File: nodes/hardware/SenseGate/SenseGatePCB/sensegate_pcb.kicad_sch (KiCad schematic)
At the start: 6 parts, among them J1 Conn_01x04_Socket, J2 Conn_01x04_Socket, J3 Conn_01x04_Socket, SW1 SW_Reed, SW2 SW_Reed, SW3 SW_Reed

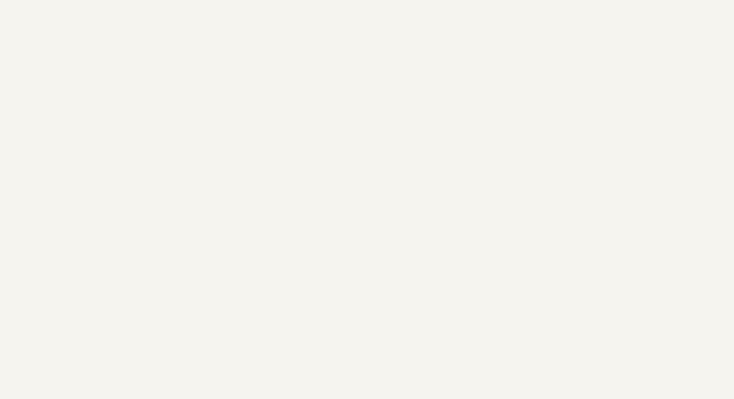
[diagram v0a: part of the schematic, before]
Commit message: added symbol for solar dcdc converter
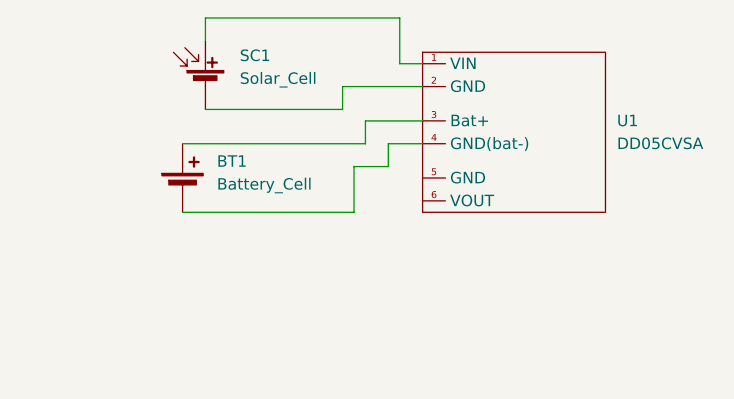
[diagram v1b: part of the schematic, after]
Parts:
- added BT1: Battery_Cell, symbol Device:Battery_Cell
- added SC1: Solar_Cell, symbol Device:Solar_Cell
- added U1: DD05CVSA, symbol custom_symbols:dd05cvsa_DCDC_Converter
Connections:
- new net: SC1.1 (+), U1.1 (VIN)
- new net: SC1.2 (-), U1.2 (GND)
- new net: BT1.1 (+), U1.3 (Bat+)
- new net: BT1.2 (-), U1.4 (GND(bat-))

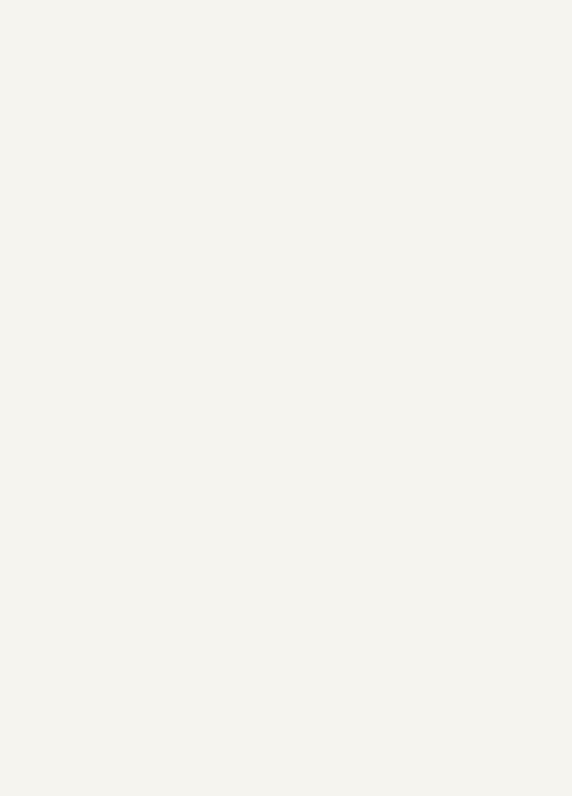
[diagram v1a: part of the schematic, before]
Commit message: added footprint with pads of sensemate to sensegate pcb
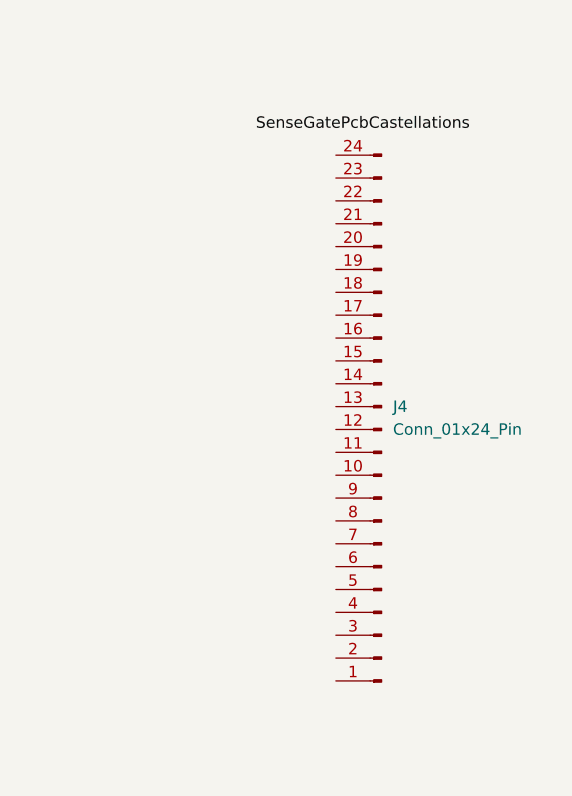
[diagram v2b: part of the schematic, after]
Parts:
- added J4: Conn_01x24_Pin, SenseGateLib:SenseMateInterface, symbol Connector:Conn_01x24_Pin
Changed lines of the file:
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@@
+		)
+	)
+	(label "SenseGatePcbCastellations"
+		(at 248.92 63.5 0)
+		(effects
+			(font
+				(size 1.27 1.27)
+			)
+			(justify left bottom)
 		)
 	)
@@
 					(unit 1)
 				)
+			)
+		)
+	)
+	(symbol
+		(lib_id "Connector:Conn_01x24_Pin")
+		(at 262.89 96.52 180)
+		(unit 1)
+		(body_style 1)
+		(exclude_from_sim no)
+		(in_bom yes)
+		(on_board yes)
+		(in_pos_files yes)
+		(dnp no)
+		(fields_autoplaced yes)
+		(property "Reference" "J4"
+			(at 264.16 93.9799 0)
+			(show_name no)
+			(do_not_autoplace no)
+			(effects
+				(font
+					(size 1.27 1.27)
+				)
+				(justify right)
+			)
+		)
+		(property "Value" "Conn_01x24_Pin"
+			(at 264.16 96.5199 0)
+			(show_name no)
+			(do_not_autoplace no)
+			(effects
+				(font
+					(size 1.27 1.27)
+				)
+				(justify right)
+			)
+		)
+		(property "Footprint" "SenseGateLib:SenseMateInterface"
+			(at 262.89 96.52 0)
+			(hide yes)
+			(show_name no)
+			(do_not_autoplace no)
+			(effects
+				(font
+					(size 1.27 1.27)
+				)
+			)
+		)
+		(property "Datasheet" ""
+			(at 262.89 96.52 0)
+			(hide yes)
+			(show_name no)
+			(do_not_autoplace no)
+			(effects
+				(font
+					(size 1.27 1.27)
+				)
+			)
+		)
+		(property "Description" "Generic connector, single row, 01x24, script generated"
+			(at 262.89 96.52 0)
+			(hide yes)
+			(show_name no)
+			(do_not_autoplace no)
+			(effects
+				(font
+					(size 1.27 1.27)
+				)
+			)
+		)
+		(pin "11"
+		)
+		(pin "4"
+		)
+		(pin "2"
+		)
+		(pin "5"
+		)
+		(pin "3"
+		)
+		(pin "6"
+		)
+		(pin "7"
+		)
+		(pin "8"
+		)
+		(pin "1"
+		)
+		(pin "9"
+		)
+		(pin "10"
+		)
+		(pin "14"
+		)
+		(pin "15"
+		)
+		(pin "12"
+		)
+		(pin "23"
+		)
+		(pin "20"
+		)
+		(pin "17"
+		)
+		(pin "22"
+		)
+		(pin "19"
+		)
+		(pin "16"
+		)
+		(pin "13"
+		)
+		(pin "18"
+		)
+		(pin "21"
+		)
+		(pin "24"
+		)
+		(instances
+			(project "sensegate_pcb"
+				(path "/cab49cbb-a41f-4356-a83b-79a7aa8374de"
+					(reference "J4")
+					(unit 1)
+				)

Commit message: added solar boost converter footprint
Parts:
- U1: footprint (none) -> custom_dcdc_converters:DD05CVSA
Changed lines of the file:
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@@
 			)
 		)
-		(property "Footprint" ""
+		(property "Footprint" "custom_dcdc_converters:DD05CVSA"
 			(at 167.64 53.34 0)
 			(hide yes)
